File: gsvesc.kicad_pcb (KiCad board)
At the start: 4 copper layers, 111 x 111 mm, 113 parts, among them J1 Conn_01x06, J10 PHASE_C, J11 PHASE_A, J12 NTC, J13 PHASE_B, J14 Conn_02x04_Odd_Even, J2 Conn_01x06, J3 Conn_01x06, J4 Conn_01x05, J5 Conn_01x03, J6 USB_B_Mini, J7 BAT+, J8 BAT-, Q1 NVMFS5C604, Q2 NVMFS5C604, Q3 NVMFS5C604, Q4 NVMFS5C604, Q5 NVMFS5C604, Q6 NVMFS5C604, U1 STM32F405RGTx, U2 IRU1010-33, U3 DRV8301DCAR, U4 AD8418, U5 AD8418, U6 AD8418, Y1 ABM3B 8MHz

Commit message: gsesc v3, work in progress
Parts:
- added C14: 1n00, Capacitor_SMD:C_0805_2012Metric, F.Cu at (92.6, 72.2)
- added C24: 1n00, Capacitor_SMD:C_0805_2012Metric, F.Cu at (80.7, 72.1)
- added C45: 680u/80V, Capacitor_THT:CP_Radial_D12.5mm_P5.00mm, F.Cu at (128.9, 98.3)
- added C46: 680u/80V, Capacitor_THT:CP_Radial_D12.5mm_P5.00mm, F.Cu at (145.5, 98.0)
- added C47: 1n00, Capacitor_SMD:C_0805_2012Metric, F.Cu at (73.1, 77.0)
- added D5: D, Diode_SMD:D_SMA, F.Cu at (62.2, 85.0)
- added H1: MountingHole, MountingHole:MountingHole_3.2mm_M3, F.Cu at (100.0, 48.5)
- added H2: MountingHole, MountingHole:MountingHole_3.2mm_M3, F.Cu at (144.6, 125.8)
- added H3: MountingHole, MountingHole:MountingHole_3.2mm_M3, F.Cu at (55.4, 125.8)
- added U7: M74VHC1GT66DTT1G, gsvesc:M74VHC1GT66DTT1G, F.Cu at (92.6, 68.2)
- added U8: M74VHC1GT66DTT1G, gsvesc:M74VHC1GT66DTT1G, F.Cu at (80.5, 67.9)
- added U9: M74VHC1GT66DTT1G, gsvesc:M74VHC1GT66DTT1G, F.Cu at (68.0, 74.4)
- C13, C15, C17, C18, C20, C5, C7, C8, C9, R10, R11, R14, R16, R31, R32, R37, R41, R9: moved to F.Cu
- C35, C40, C41: value 4n70 -> 1n00
- C36, C37, C43: value 47u0/100V -> 10u0/100V; moved to F.Cu
- J10, J11, J13, J7, J8: footprint Connector_Wire:SolderWirePad_1x01_SMD_5x10mm -> gsvesc:TestPoint_Pad_5.0x5.0mm
- R25, R26, R27, R28, R34, R35: moved to B.Cu
- R29, R30, R33: value 100R -> 1k00
- moved J7 93.4 mm to (155.4, 28.8)
- moved J8 82.3 mm to (138.2, 16.8)
- moved J5 76.9 mm to (125.9, 146.1), turned to 220 degrees
- moved J2 76.1 mm to (131.4, 175.4), turned to 140 degrees
- moved R5 69.5 mm to (118.5, 144.8)
- moved C1 68.5 mm to (122.1, 141.7), turned to 40 degrees
- moved J6 56.1 mm to (63.6, 139.9), turned to 320 degrees
- moved R2 54.3 mm to (69.0, 138.8), turned to 230 degrees
- moved R10 54.1 mm to (85.7, 146.5), turned to 65 degrees
- moved R1 51.8 mm to (65.5, 135.7), turned to 230 degrees
- moved D2 51.6 mm to (83.4, 145.5), turned to 65 degrees
- moved R11 51.3 mm to (81.2, 144.4), turned to 65 degrees
- moved C9 50.3 mm to (74.0, 137.0), turned to 0 degrees
- moved R3 50.3 mm to (67.3, 137.2), turned to 230 degrees
- moved R9 49.1 mm to (77.0, 142.5), turned to 65 degrees
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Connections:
- net /POWER_CTRL/SUPPLY renamed /DRV8301/VBAT
- C3 pad 2: Net-(C3-Pad2) -> GND
- C41 pad 1: /MCU/CURRENT_1 -> Net-(C41-Pad1)
- J14 pad 4: Net-(J14-Pad4) -> /NRF/GPIO1
- J14 pad 6: Net-(J14-Pad6) -> /NRF/GPIO2
- J14 pad 8: Net-(J14-Pad8) -> /NRF/GPIO3
- J3 pad 3: Net-(J3-Pad3) -> /MCU/PC5
- U1 pad 28: /MCU/PB2 -> /NRF/GPIO1
- U1 pad 54: /MCU/PD2 -> /POWER/CURR_FILTER
- U1 pad 55: /MCU/PB3 -> /NRF/GPIO2
- U1 pad 56: /MCU/PB4 -> /NRF/GPIO3
- U1 pad 6: GND -> Net-(C4-Pad2)
- Y1 pad 1: GND -> Net-(C4-Pad2)
- Y1 pad 2: Net-(C3-Pad2) -> GND
- Y1 pad 4: Net-(C4-Pad2) -> GND
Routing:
- net GND: track 96.5 -> 0.00 mm, vias 212 -> 0
- net /MCU/TEMP_MOTOR: track 73.3 -> 0.00 mm, vias 2 -> 0
- net /MCU/ADC_TEMP: track 70.7 -> 0.00 mm, vias 2 -> 0
- net /MCU/CURRENT_3: track 69.3 -> 0.00 mm, vias 2 -> 0
- net /MCU/HALL_3: track 66.1 -> 0.00 mm
- net /MCU/HALL_2: track 64.8 -> 0.00 mm
- net /MCU/HALL_1: track 63.5 -> 0.00 mm
- net /MCU/HALL_ROT_B: track 63.3 -> 0.00 mm, vias 1 -> 0
- net /MCU/HALL_ROT_A: track 62.5 -> 0.00 mm, vias 1 -> 0
- net /MCU/HALL_TRIG: track 62.2 -> 0.00 mm, vias 1 -> 0
- net VCC: track 57.0 -> 0.00 mm, vias 26 -> 0
- net /DRV8301/GL_C: track 56.3 -> 0.00 mm
- net /DRV8301/SH_C: track 56.1 -> 0.00 mm, vias 3 -> 0
- net /MCU/CURRENT_2: track 54.6 -> 0.00 mm, vias 2 -> 0
- net /DRV8301/SENS_C: track 53.8 -> 0.00 mm, vias 2 -> 0
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- removed copper zone on F.Cu, net +5V
- removed copper zone on B.Cu, net /DRV8301/SH_A
- removed copper zone on B.Cu, net /DRV8301/SH_B
- removed copper zone on B.Cu, net /DRV8301/SH_C
- removed copper zone on B.Cu, net /DRV8301/VBAT
- removed copper zone on F.Cu, net /DRV8301/VBAT
- removed copper zone on B.Cu, net /POWER/PHASE_A
- removed copper zone on B.Cu, net /POWER/PHASE_B
- removed copper zone on B.Cu, net /POWER/PHASE_C
- removed copper zone on B.Cu, net GND
- removed copper zone on F.Cu, net GND
- removed copper zone on In2.Cu, net GND
- removed copper zone on F.Cu, net Net-(C27-Pad1)
- removed copper zone on F.Cu, net VCC
- removed copper zone on In1.Cu, net VCC
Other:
- board size 111 x 111 mm -> 115 x 115 mm
- rule via_min_size: 0.4 -> 0.6

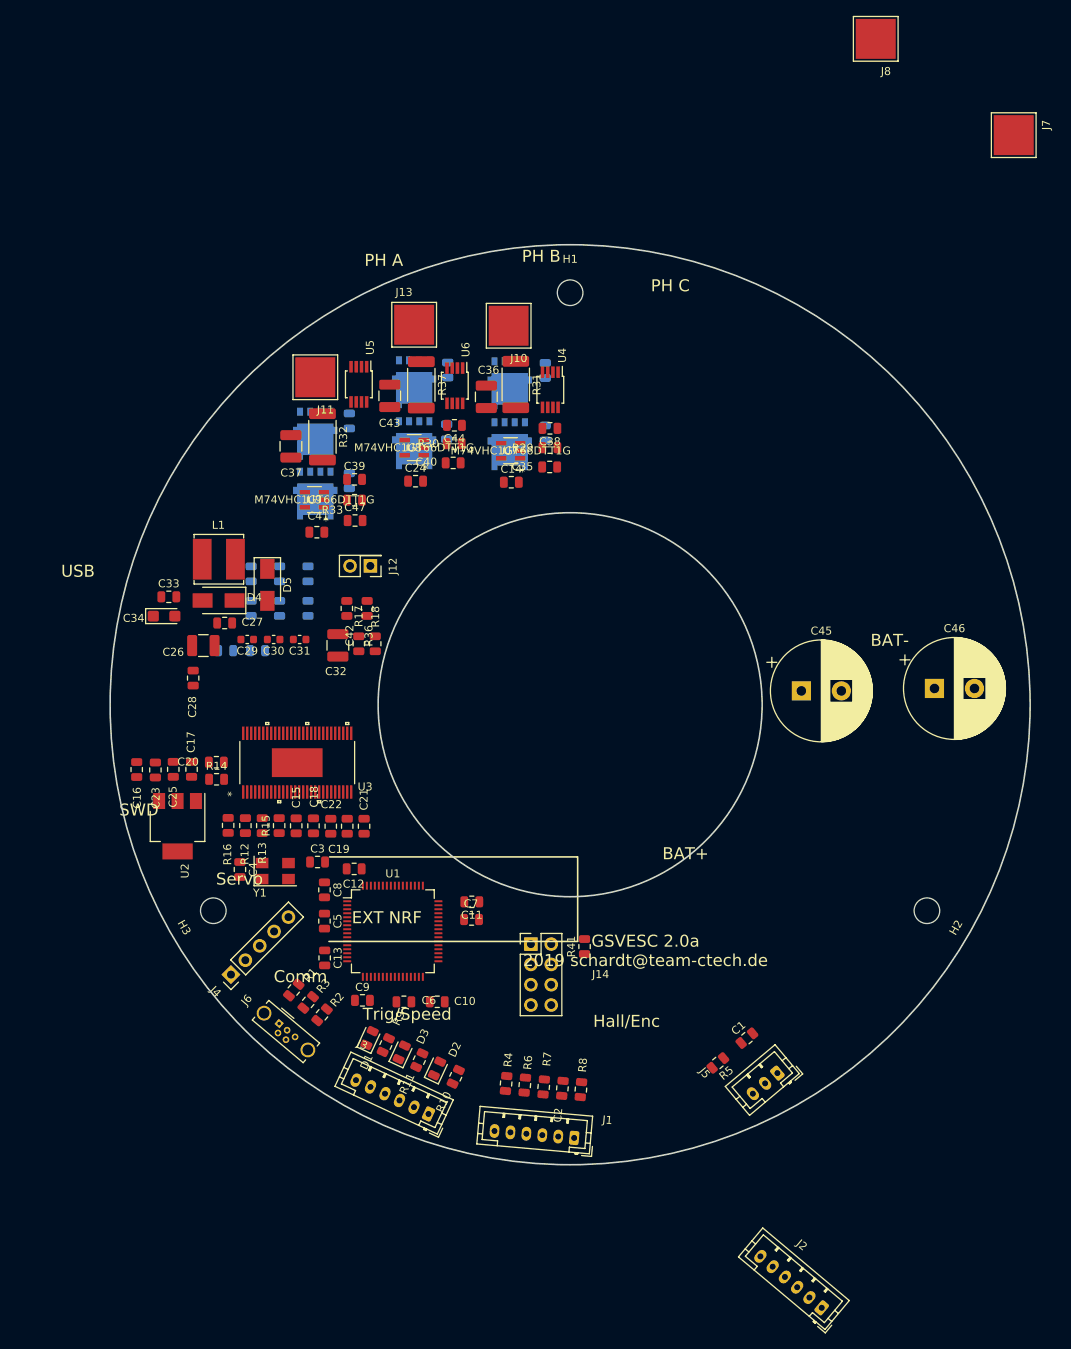
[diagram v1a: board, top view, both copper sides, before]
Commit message: library wieder im projektordner
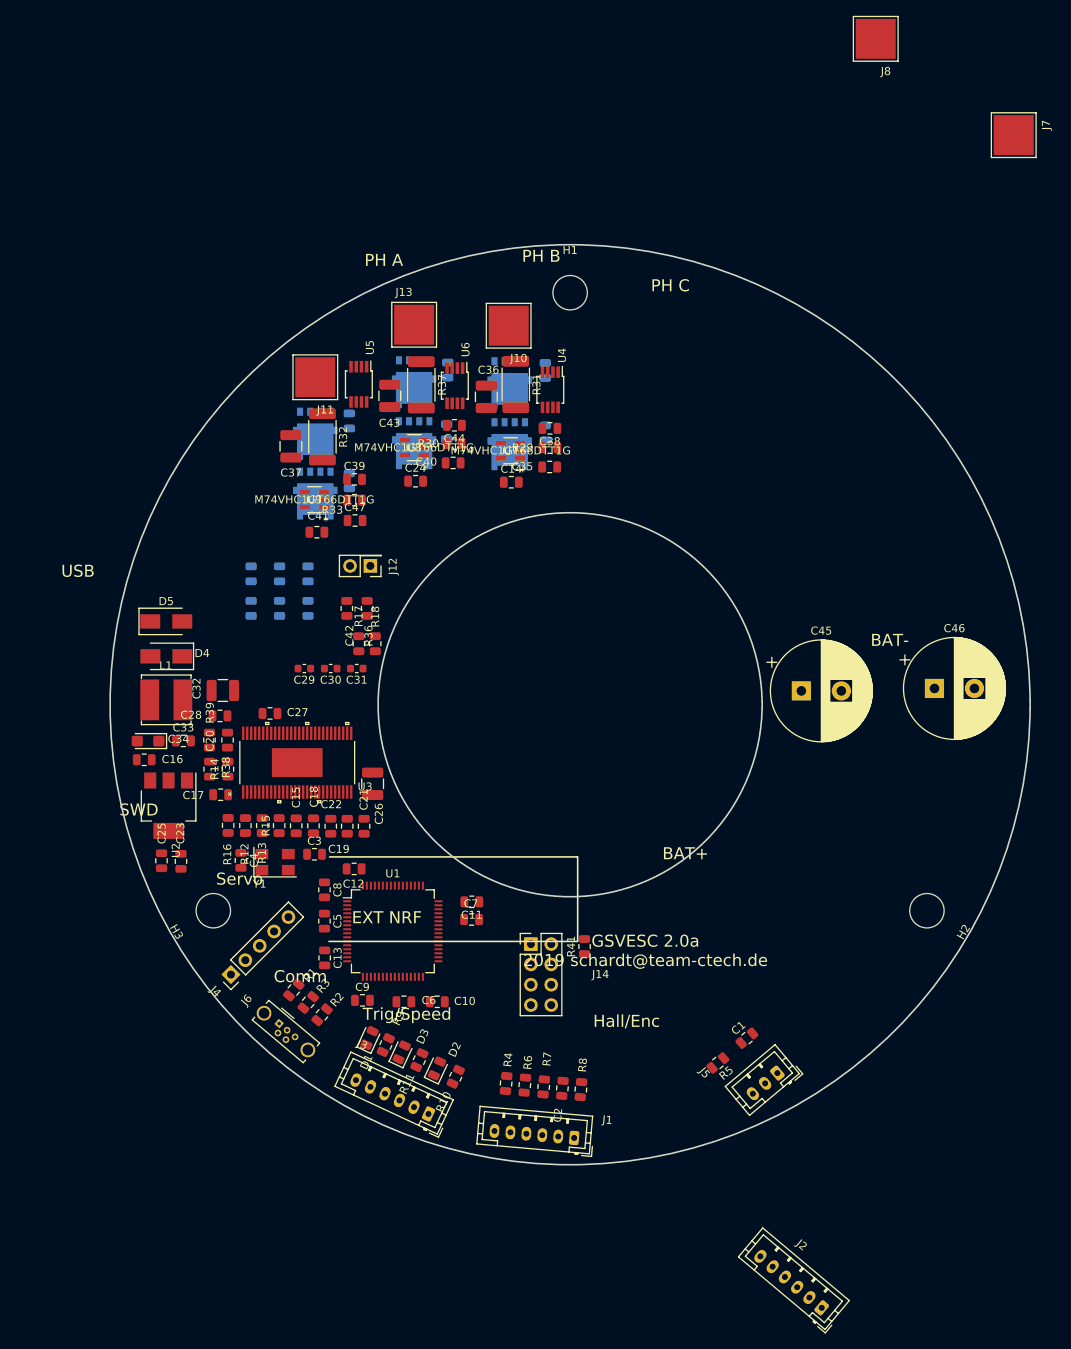
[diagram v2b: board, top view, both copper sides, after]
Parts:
- H1, H2, H3: footprint MountingHole:MountingHole_3.2mm_M3 -> MountingHole:MountingHole_4.3mm_M4
- R38, R39: moved to F.Cu
- moved C26 27.3 mm to (75.3, 109.9), turned to 270 degrees
- moved L1 18.8 mm to (49.5, 99.4)
- moved C33 18.1 mm to (51.7, 104.5)
- moved C34 15.7 mm to (47.2, 104.5), turned to 180 degrees
- moved C32 15.4 mm to (56.6, 98.2), turned to 180 degrees
- moved D5 13.4 mm to (49.5, 89.6), turned to 0 degrees
- moved R39 12.7 mm to (54.9, 104.4), turned to 90 degrees
- moved C27 12.6 mm to (62.5, 101.1)
- moved C23 11.9 mm to (51.4, 119.6), turned to 270 degrees
- moved C25 11.5 mm to (48.9, 119.5), turned to 270 degrees
- moved R38 11.2 mm to (57.2, 104.4), turned to 270 degrees
- moved D4 9.56 mm to (49.5, 94.0)
- moved C29 8.01 mm to (66.8, 95.5)
- moved C30 8.01 mm to (70.1, 95.5)
- moved C31 8.01 mm to (73.3, 95.5)
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
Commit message: Update
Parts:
- C26, C32: value 47u0/100V -> 10u0/100V
- C45, C46: value 680u/80V -> 680u/63V
- D5: value D -> SMBJ6.0CA; footprint Diode_SMD:D_SMA -> Diode_SMD:D_SMB
- H1, H2, H3: footprint MountingHole:MountingHole_4.3mm_M4 -> MountingHole:MountingHole_3.2mm_M3
- R19, R20, R21, R22, R23, R24: moved to F.Cu
- moved J7 110.9 mm to (57.6, 80.9)
- moved J8 98.4 mm to (57.6, 73.2)
- moved C46 53.2 mm to (115.4, 54.2), turned to 240 degrees
- moved C45 35.0 mm to (107.1, 70.9), turned to 60 degrees
- moved R36 30.1 mm to (68.6, 58.4)
- moved J2 29.4 mm to (118.1, 149.3), turned to 195 degrees
- moved C42 29.1 mm to (66.2, 59.4)
- moved J12 24.4 mm to (72.1, 58.5), turned to 90 degrees
- moved R17 23.7 mm to (78.5, 115.6)
- moved C35 23.4 mm to (86.5, 49.6)
- moved R18 23.2 mm to (76.2, 115.5), turned to 270 degrees
- moved C14 21.2 mm to (86.5, 51.9), turned to 180 degrees
- moved U7 19.5 mm to (91.0, 48.8), turned to 0 degrees
- moved J11 17.6 mm to (76.5, 74.6)
- moved R29 17.4 mm to (85.8, 55.0), turned to 90 degrees
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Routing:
- net /MCU/ADC_TEMP: track 0.00 -> 93.4 mm, vias 0 -> 2
- net /MCU/CURRENT_3: track 0.00 -> 93.2 mm, vias 0 -> 2
- net /POWER/CURR_FILTER: track 0.00 -> 91.1 mm, vias 0 -> 4
- net /MCU/CURRENT_2: track 0.00 -> 78.8 mm, vias 0 -> 2
- net /MCU/CURRENT_1: track 0.00 -> 75.8 mm, vias 0 -> 2
- net VCC: track 0.00 -> 67.5 mm, vias 0 -> 26
- net /MCU/SERVO: track 0.00 -> 60.8 mm, vias 0 -> 2
- net /DRV8301/GL_C: track 0.00 -> 58.8 mm, vias 0 -> 2
- net /DRV8301/SH_C: track 0.00 -> 50.9 mm, vias 0 -> 27
- net /DRV8301/GH_C: track 0.00 -> 50.0 mm, vias 0 -> 2
- net /MCU/RX_SDA_NSS: track 0.00 -> 49.0 mm, vias 0 -> 1
- net /DRV8301/SENS_C: track 0.00 -> 47.8 mm, vias 0 -> 2
- net /DRV8301/GL_B: track 0.00 -> 46.1 mm, vias 0 -> 2
- net /DRV8301/SENS_B: track 0.00 -> 45.5 mm, vias 0 -> 2
- net /MCU/SCK_ADC_EXT: track 0.00 -> 44.3 mm, vias 0 -> 1
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- added copper zone on B.Cu, net +5V
- added copper zone on F.Cu, net +5V
- added copper zone on B.Cu, net /DRV8301/SH_A
- added copper zone on F.Cu, net /DRV8301/SH_A
- added copper zone on In1.Cu, net /DRV8301/SH_A
- added copper zone on In2.Cu, net /DRV8301/SH_A
- added copper zone on B.Cu, net /DRV8301/SH_B
- added copper zone on F.Cu, net /DRV8301/SH_B
- added copper zone on In1.Cu, net /DRV8301/SH_B
- added copper zone on In2.Cu, net /DRV8301/SH_B
- added copper zone on B.Cu, net /DRV8301/SH_C
- added copper zone on F.Cu, net /DRV8301/SH_C
- added copper zone on In1.Cu, net /DRV8301/SH_C
- added copper zone on In2.Cu, net /DRV8301/SH_C
- added copper zone on B.Cu, net /DRV8301/VBAT
- added copper zone on F.Cu, net /DRV8301/VBAT
- added copper zone on In1.Cu, net /DRV8301/VBAT
- added copper zone on In2.Cu, net /DRV8301/VBAT
- added copper zone on F.Cu, net /POWER/PHASE_A
- added copper zone on F.Cu, net /POWER/PHASE_B
- added copper zone on F.Cu, net /POWER/PHASE_C
- added copper zone on B.Cu, net GND
- added copper zone on F.Cu, net GND
- added copper zone on In1.Cu, net GND
- added copper zone on In2.Cu, net GND
- added copper zone on F.Cu, net Net-(C27-Pad1)
- added copper zone on F.Cu, net VCC
- added copper zone on In2.Cu, net VCC
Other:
- board size 115 x 115 mm -> 111 x 111 mm
- net class Default: trace_width 0.2 -> 0.15
- net class POWER added: clearance 0.15, trace_width 0.2, via_dia 0.6, via_drill 0.3
